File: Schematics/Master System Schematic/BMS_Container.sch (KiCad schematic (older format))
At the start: 8 parts, among them K1 Cooling Pump Shutoff Relay, K53 BMS_PWR_Relay, K54 Cooling Pump Relay, K55 BMS_FanControl, U6 OrionBMS2

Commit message: fixed therm boards
fixed therm board implementation
beginning accumulator redraw
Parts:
- removed K55: BMS_FanControl, Relay_THT:Relay_SPST_StandexMeder_MS_Form1AB, symbol Relay:MSxx-1Bxx-75
- added K?: BMS_Fan_Relay, Relay_THT:Relay_StandexMeder_DIP_LowProfile, symbol Relay:DIPxx-1Axx-11x
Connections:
- net CoolingPumpControl is gone; now on net GLV(BMS): K1.1
- net BMS_Fan: now also K?.1, K?.14
- net GLV(BMS): now also K?.2, K?.7, K?.8
- net at R10.1, U6.10 (MPOut3/Fan_En): now also K?.6
- net at U6.3 (RM2+): now also K53.7, K53.8
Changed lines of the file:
@@
 Wire Wire Line
 	5850 4900 5350 4900
-Wire Wire Line
-	9850 3200 9850 2800
-Text HLabel 4800 3200 0    50   Input ~ 0
-CoolingPumpControl
 Text HLabel 14100 2000 2    50   Input ~ 0
 CAN_H(Charger)
@@
 Wire Wire Line
 	4850 2000 5150 2000
-Wire Wire Line
-	9850 2800 9850 1550
-Connection ~ 9850 2800
 Connection ~ 9850 1550
 Wire Wire Line
@@
 Wire Wire Line
 	5750 1550 9850 1550
-Wire Wire Line
-	6550 1650 6550 4100
 Connection ~ 6550 4100
 Wire Wire Line
@@
 	9850 1550 14100 1550
 Wire Wire Line
-	4800 3200 8350 3200
-Wire Wire Line
 	4800 3600 8000 3600
 Wire Wire Line
@@
 Wire Wire Line
 	6700 5600 4150 5600
-$Comp
-L Relay:MSxx-1Bxx-75 K?
-U 1 1 6454A212
-P 3400 5800
-AR Path="/5F45B05E/6454A212" Ref="K?"  Part="1"
-AR Path="/6454A212" Ref="K?"  Part="1"
-AR Path="/60D53BFB/6454A212" Ref="K55"  Part="1"
-F 0 "K55" V 2833 5800 50  0000 C CNN
-F 1 "BMS_FanControl" V 2924 5800 50  0000 C CNN
-F 2 "Relay_THT:Relay_SPST_StandexMeder_MS_Form1AB" H 3750 5750 50  0001 L CNN
-F 3 "https://standexelectronics.com/de/produkte/ms-reed-relais/" H 3400 5800 50  0001 C CNN
-	1    3400 5800
-	0    1    1    0
-$EndComp
 Text HLabel 2900 6000 0    50   Output ~ 0
 BMS_Fan
@@
 Wire Wire Line
 	2900 4900 4950 4900
+Connection ~ 4950 4900
+Wire Wire Line
+	4950 4900 4950 1650
+$Comp
+L Relay:DIPxx-1Axx-11x K?
+U 1 1 5FB9D72C
+P 3400 5800
+F 0 "K?" V 3850 5850 50  0000 R CNN
+F 1 "BMS_Fan_Relay" V 3750 6100 50  0000 R CNN
+F 2 "Relay_THT:Relay_StandexMeder_DIP_LowProfile" H 3750 5750 50  0001 L CNN
+F 3 "https://standexelectronics.com/wp-content/uploads/datasheet_reed_relay_DIP.pdf" H 3400 5800 50  0001 C CNN
+	1    3400 5800
+	0    1    1    0
+$EndComp
+Wire Wire Line
+	8350 3200 6550 3200
+Wire Wire Line
+	9850 1550 9850 2800
+Wire Wire Line
+	6550 1650 6550 3200
+Connection ~ 6550 3200
+Wire Wire Line
+	6550 3200 6550 4100
+Connection ~ 9850 2800
+Wire Wire Line
+	9850 2800 9850 3200
 Wire Bus Line
 	8850 8500 8850 8800
@@
 Wire Bus Line
 	8850 7550 8850 7850
-Connection ~ 4950 4900
-Wire Wire Line
-	4950 4900 4950 1650
 $EndSCHEMATC

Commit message: roughly spread out accumulator components, updated therms boards
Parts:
- gave numbers to parts that had none: 1
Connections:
- net at U6.3 (RM2+): now also K53.7, K53.8
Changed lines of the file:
@@
 	4950 4900 4950 1650
 $Comp
-L Relay:DIPxx-1Axx-11x K?
+L Relay:DIPxx-1Axx-11x K55
 U 1 1 5FB9D72C
 P 3400 5800
-F 0 "K?" V 3850 5850 50  0000 R CNN
+F 0 "K55" V 3850 5850 50  0000 R CNN
 F 1 "BMS_Fan_Relay" V 3750 6100 50  0000 R CNN
 F 2 "Relay_THT:Relay_StandexMeder_DIP_LowProfile" H 3750 5750 50  0001 L CNN

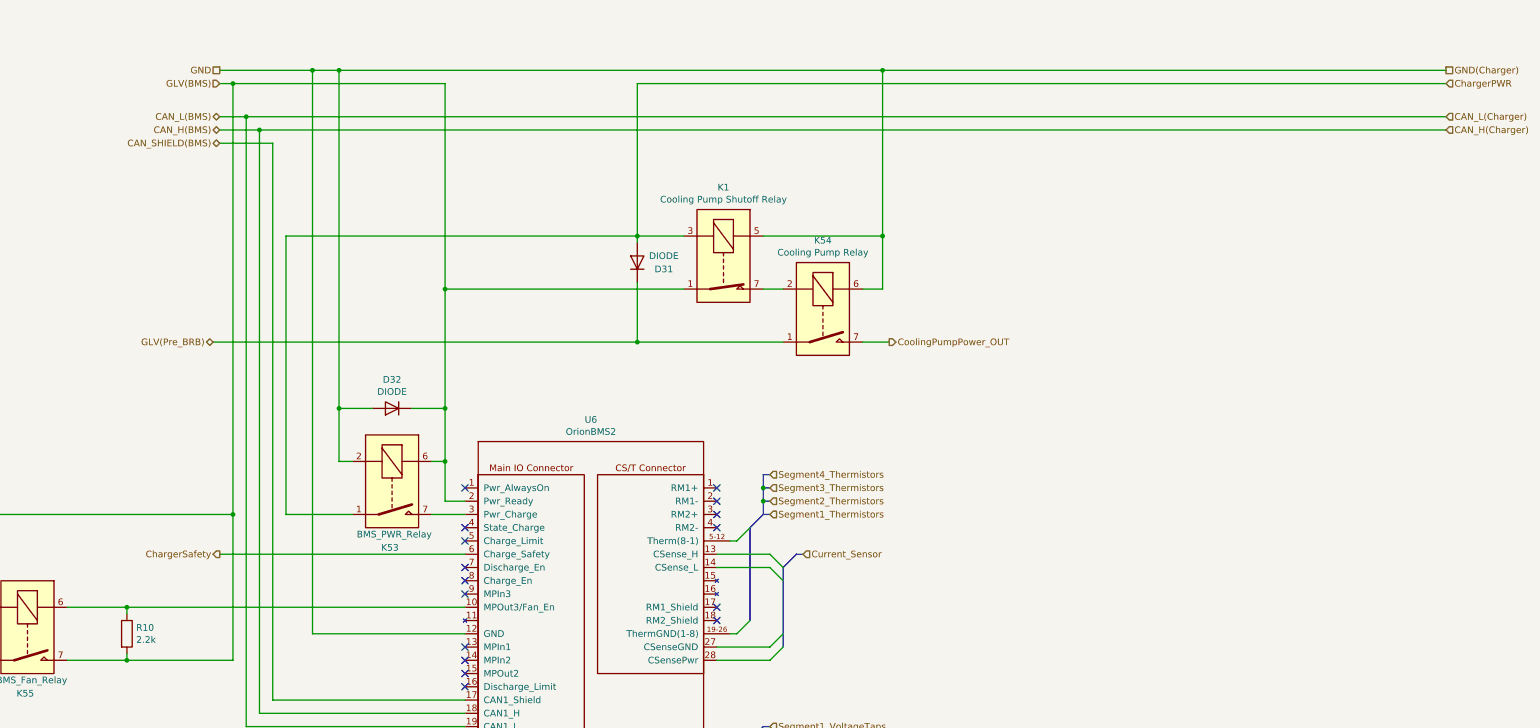
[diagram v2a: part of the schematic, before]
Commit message: Added Thermistor Expansion connection
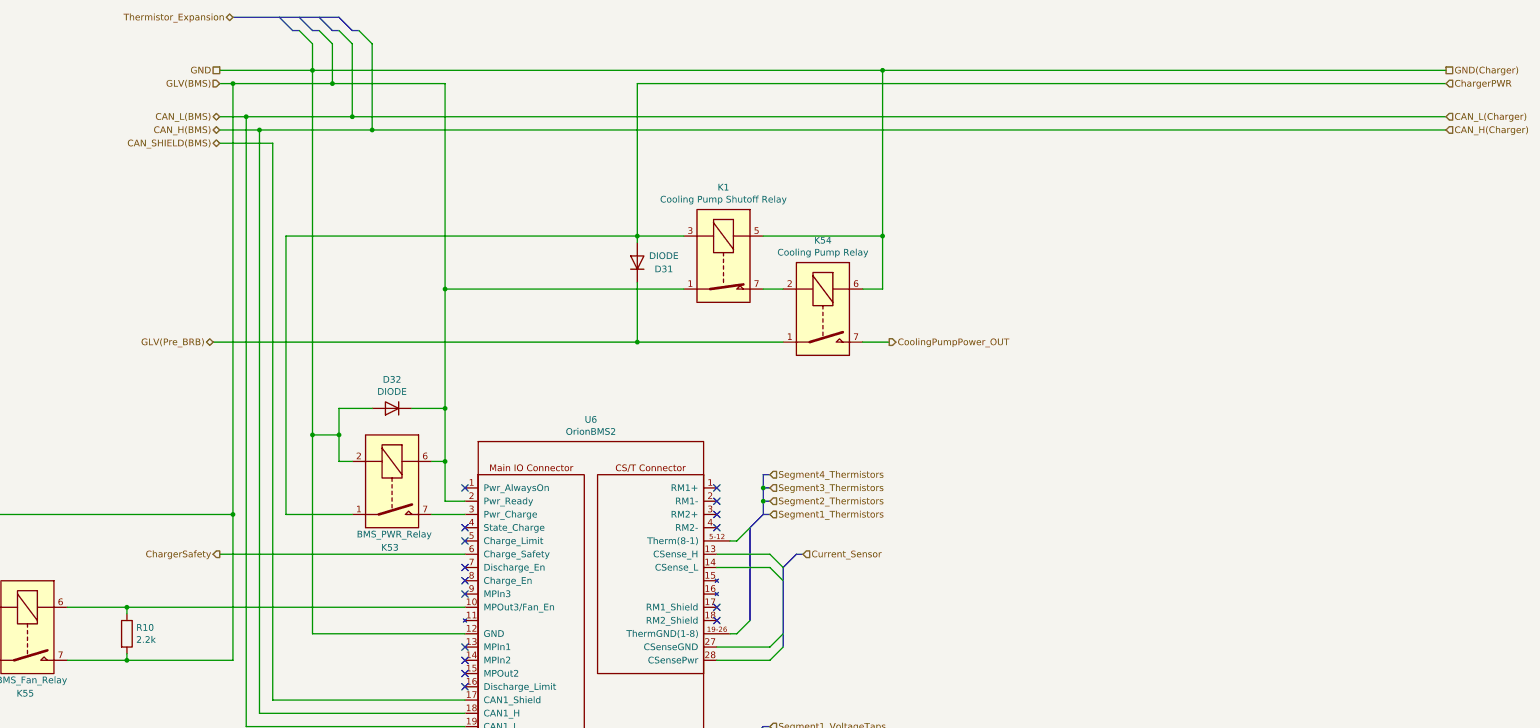
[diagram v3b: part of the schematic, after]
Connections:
- net at U6.3 (RM2+): now also K53.7, K53.8
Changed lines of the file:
@@
 	6000 4100 5750 4100
 Wire Wire Line
-	5750 4100 5750 4500
+	5750 4100 5750 4300
 Wire Wire Line
 	5750 4500 5850 4500
@@
 Connection ~ 5050 1900
 Wire Wire Line
-	5550 1550 5550 5800
+	5550 1550 5550 4300
 Connection ~ 5550 1550
 Wire Wire Line
-	5550 1550 5750 1550
-Wire Wire Line
 	4850 1650 4950 1650
-Wire Wire Line
-	5750 1550 5750 4100
-Connection ~ 5750 1550
-Connection ~ 5750 4100
-Wire Wire Line
-	5750 1550 9850 1550
 Connection ~ 6550 4100
 Wire Wire Line
-	5150 2000 14100 2000
-Wire Wire Line
-	5050 1900 14100 1900
-Wire Wire Line
-	9850 1550 14100 1550
-Wire Wire Line
 	4800 3600 8000 3600
 Wire Wire Line
 	8000 1650 8000 2800
-Wire Wire Line
-	8000 1650 14100 1650
 Wire Wire Line
 	6700 5600 4150 5600
@@
 	4950 6000 4950 4900
 Connection ~ 4950 1650
-Wire Wire Line
-	4950 1650 6550 1650
 $Comp
 L Device:R R10
@@
 Wire Wire Line
 	9850 2800 9850 3200
+Text HLabel 4950 1150 0    50   BiDi ~ 0
+Thermistor_Expansion
+Entry Bus Bus
+	5300 1150 5400 1250
+Entry Bus Bus
+	5450 1150 5550 1250
+Entry Wire Line
+	5550 1350 5450 1250
+Entry Wire Line
+	5700 1350 5600 1250
+Wire Bus Line
+	5600 1250 5550 1250
+Wire Bus Line
+	5450 1250 5400 1250
+Entry Bus Bus
+	5600 1150 5700 1250
+Entry Bus Bus
+	5750 1150 5850 1250
+Entry Wire Line
+	5850 1350 5750 1250
+Entry Wire Line
+	6000 1350 5900 1250
+Wire Bus Line
+	5900 1250 5850 1250
+Wire Bus Line
+	5750 1250 5700 1250
+Wire Wire Line
+	9850 1550 14100 1550
+Wire Wire Line
+	8000 1650 14100 1650
+Wire Wire Line
+	4950 1650 5700 1650
+Wire Wire Line
+	5150 2000 6000 2000
+Wire Wire Line
+	5050 1900 5850 1900
+Wire Wire Line
+	5550 1350 5550 1550
+Wire Wire Line
+	5700 1350 5700 1650
+Wire Wire Line
+	5850 1350 5850 1900
+Wire Wire Line
+	6000 1350 6000 2000
+Connection ~ 5700 1650
+Connection ~ 5850 1900
+Connection ~ 6000 2000
+Wire Wire Line
+	5700 1650 6550 1650
+Wire Wire Line
+	5850 1900 14100 1900
+Wire Wire Line
+	6000 2000 14100 2000
+Wire Wire Line
+	5750 4300 5550 4300
 Wire Bus Line
 	8850 8500 8850 8800
@@
 Wire Bus Line
 	8850 7550 8850 7850
+Wire Bus Line
+	4950 1150 5750 1150
+Connection ~ 5750 4300
+Wire Wire Line
+	5750 4300 5750 4500
+Connection ~ 5550 4300
+Wire Wire Line
+	5550 4300 5550 5800
+Wire Wire Line
+	5550 1550 9850 1550
 $EndSCHEMATC

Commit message: Master cleanup
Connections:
- net at U6.3 (RM2+): now also K53.7, K53.8
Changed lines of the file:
@@
 Wire Wire Line
 	5750 4300 5550 4300
+Connection ~ 5750 4300
+Wire Wire Line
+	5750 4300 5750 4500
+Connection ~ 5550 4300
+Wire Wire Line
+	5550 4300 5550 5800
+Wire Wire Line
+	5550 1550 9850 1550
 Wire Bus Line
 	8850 8500 8850 8800
@@
 Wire Bus Line
 	4950 1150 5750 1150
-Connection ~ 5750 4300
-Wire Wire Line
-	5750 4300 5750 4500
-Connection ~ 5550 4300
-Wire Wire Line
-	5550 4300 5550 5800
-Wire Wire Line
-	5550 1550 9850 1550
 $EndSCHEMATC

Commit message: Finished master and accum cleanup
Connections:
- net GLV(BMS) is gone; now on net GLV: D32.2 (K), K1.1, K53.6, K55.2, K55.7, K55.8, R10.2, U6.2 (RM1-)
- net GLV: now reaches U6.2 (RM1-)
- net at U6.3 (RM2+): now also K53.7, K53.8
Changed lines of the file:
@@
 $Descr B 17000 11000
 encoding utf-8
-Sheet 22 22
+Sheet 21 22
 Title "BMS & MC Container"
-Date "2020-11-11"
-Rev "6"
+Date "2020-11-12"
+Rev "7"
 Comp "Northeastern Electric Racing"
 Comment1 "https://github.com/Northeastern-Electric-Racing/NER"
@@
 CAN_L(BMS)
 Text HLabel 4850 1650 0    50   Input ~ 0
-GLV(BMS)
+GLV
 Text HLabel 4850 1550 0    50   UnSpc ~ 0
 GND

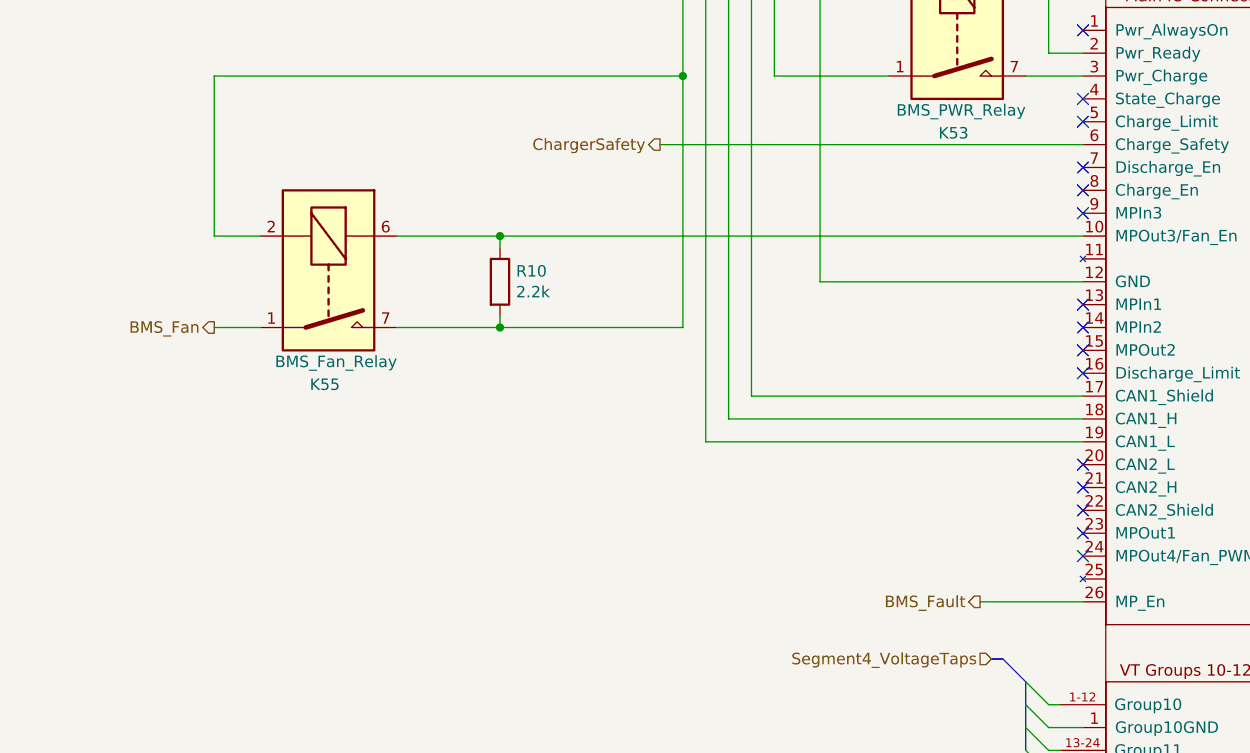
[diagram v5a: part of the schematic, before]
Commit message: added lines for charge/discharge/current limit backups
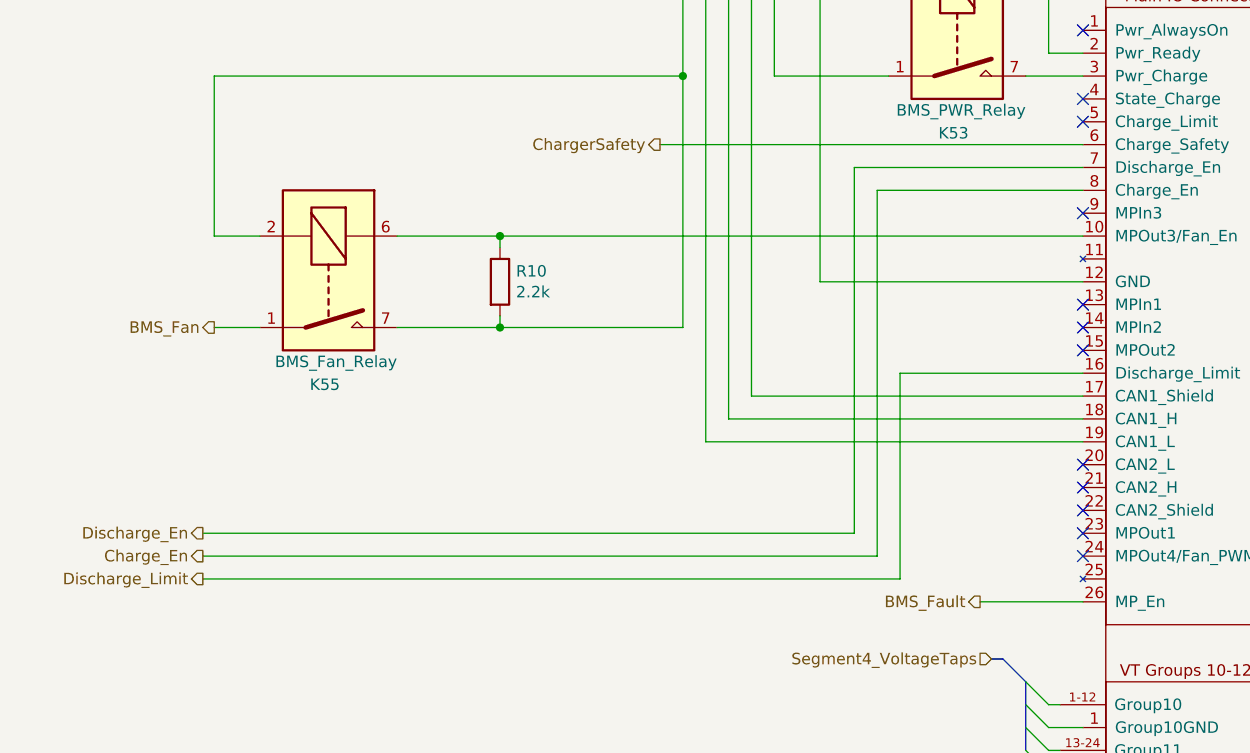
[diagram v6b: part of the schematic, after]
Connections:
- net Discharge_Limit: now reaches U6.16
- net at U6.3 (RM2+): now also K53.7, K53.8
- net Discharge_En: now reaches U6.7 (Discharge_En)
- net Charge_En: now reaches U6.8 (Charge_En)
- no-connect marks 25 -> 22
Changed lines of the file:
@@
 NoConn ~ 6700 5000
 NoConn ~ 6700 5100
-NoConn ~ 6700 5300
-NoConn ~ 6700 5400
 NoConn ~ 6700 5500
 NoConn ~ 6700 5900
 NoConn ~ 6700 6000
 NoConn ~ 6700 6100
-NoConn ~ 6700 6200
 NoConn ~ 6700 6600
 NoConn ~ 6700 6700
@@
 Wire Wire Line
 	5550 1550 9850 1550
+Wire Wire Line
+	6700 5300 5700 5300
+Wire Wire Line
+	5700 5300 5700 6900
+Wire Wire Line
+	5700 6900 2850 6900
+Wire Wire Line
+	6700 5400 5800 5400
+Wire Wire Line
+	5800 5400 5800 7000
+Wire Wire Line
+	5800 7000 2850 7000
+Wire Wire Line
+	6700 6200 5900 6200
+Wire Wire Line
+	5900 6200 5900 7100
+Wire Wire Line
+	5900 7100 2850 7100
 Wire Bus Line
 	8850 8500 8850 8800
@@
 Wire Bus Line
 	4950 1150 5750 1150
+Text HLabel 2850 6900 0    50   Output ~ 0
+Discharge_En
+Text HLabel 2850 7000 0    50   Output ~ 0
+Charge_En
+Text HLabel 2850 7100 0    50   Output ~ 0
+Discharge_Limit
 $EndSCHEMATC
